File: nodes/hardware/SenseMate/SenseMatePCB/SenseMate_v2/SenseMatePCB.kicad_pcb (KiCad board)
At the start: 2 copper layers, 43.4 x 60 mm, 17 parts, among them J1 Conn_01x04, J2 Conn_02x06_Counter_Clockwise 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, J3 Conn_Coaxial, M1 Motor_DC, Q1 2SC1815, Q2 2SC1815, SW5 SW_DPDT_x2, U1 XIAO-nRF52840-Plus-SMD, U2 RFM95W-868S2

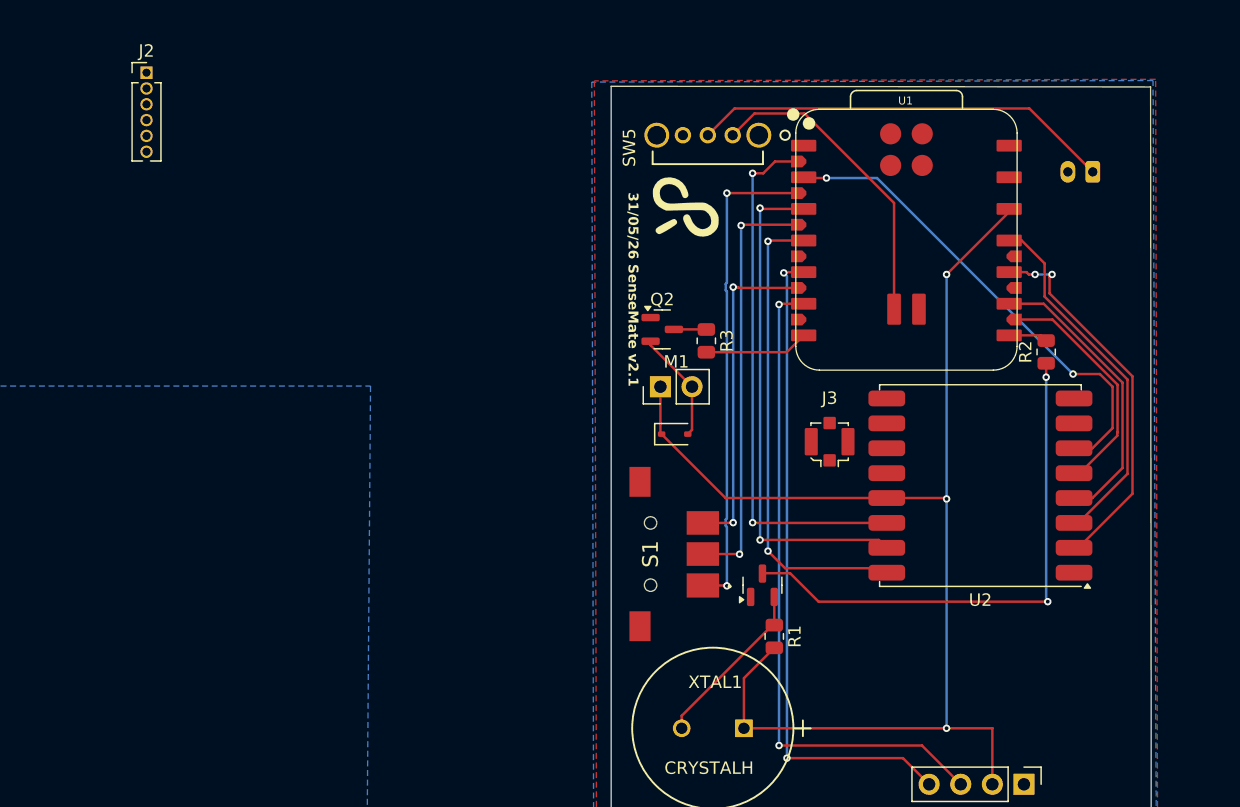
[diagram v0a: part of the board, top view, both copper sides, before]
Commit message: sensemate pcb v2.2: optimized routing further
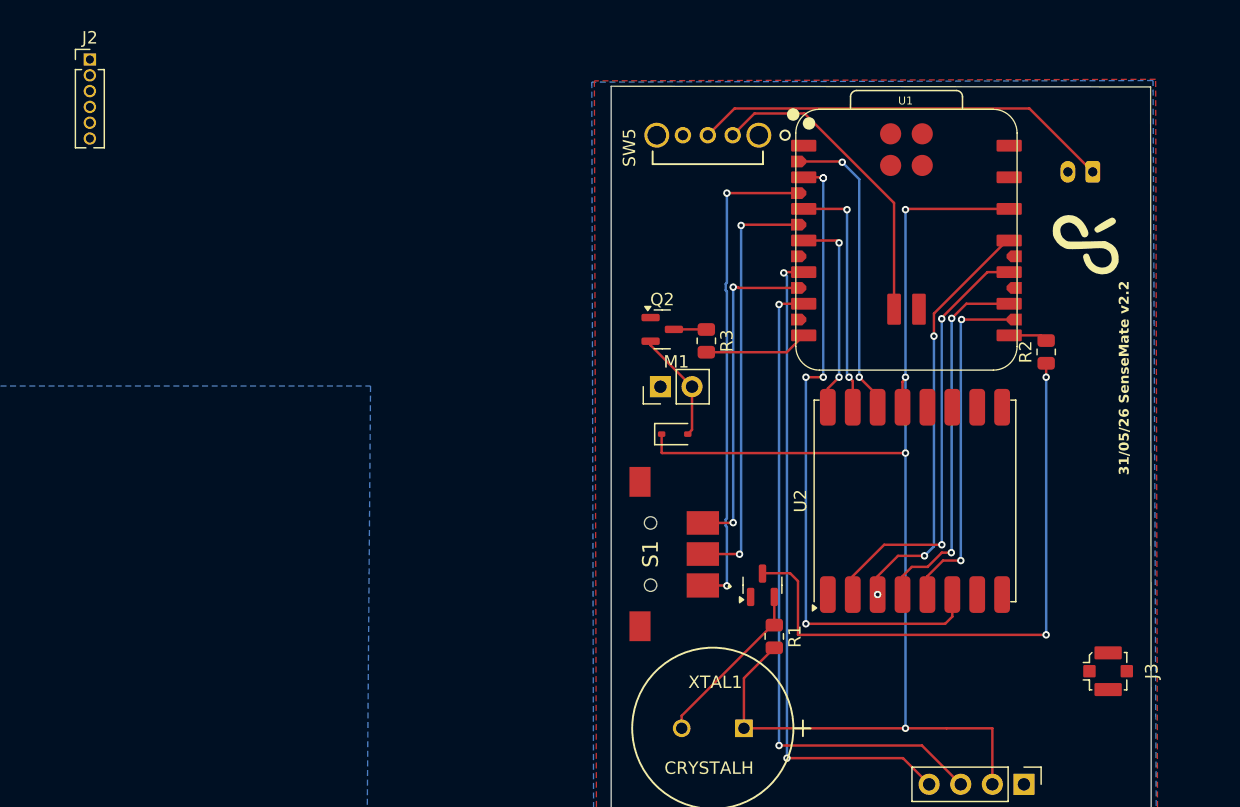
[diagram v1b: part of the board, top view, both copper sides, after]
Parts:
- moved G*** 32.2 mm to (116.5, 37.1), turned to 90 degrees
- moved J3 29.0 mm to (118.3, 73.9), turned to 90 degrees
- moved U2 5.40 mm to (102.7, 60.2), turned to 90 degrees
- moved J2 4.67 mm to (36.4, 24.8)
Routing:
- net LoRa_DIO2: track 38.1 -> 16.5 mm
- net LoRa_DIO1: track 40.6 -> 19.8 mm
- net LoRa_DIO0: track 43.0 -> 24.4 mm
- net LoRa_RST: track 38.9 -> 52.6 mm, vias 2 -> 5
- net LoRa_NSS: track 19.3 -> 28.4 mm, vias 0 -> 2
- net LoRa_SCK: track 23.5 -> 30.1 mm, vias 0 -> 2
- net Net-(Q1-B): track 43.0 -> 49.2 mm
- net LoRa_MOSI: track 29.2 -> 34.2 mm, vias 0 -> 3
- net LoRa_MISO: track 30.5 -> 34.9 mm
- net +3V3: track 104.7 -> 105.6 mm, vias 3 -> 4
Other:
- board text added: "31/05/26 SenseMate v2.2"
- board text removed: "31/05/26 SenseMate v2.1"

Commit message: Update SenseMatePCB.kicad_pcb
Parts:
- moved J3 20.7 mm to (116.2, 53.3)
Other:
- board text added: "01/06/26 SenseMate v2.2"
- board text removed: "31/05/26 SenseMate v2.2"
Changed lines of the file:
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@@
 	(footprint "Connector_Coaxial:U.FL_Molex_MCRF_73412-0110_Vertical"
 		(layer "F.Cu")
-		(at 118.261 73.914 90)
+		(at 116.181 53.34 90)
 		(descr "Molex Microcoaxial RF Connectors (MCRF), mates Hirose U.FL, (http://www.molex.com/pdm_docs/sd/734120110_sd.pdf)")
 		(tags "mcrf hirose ufl u.fl microcoaxial")
@@
 		(layer "Edge.Cuts")
 	)
-	(gr_text "31/05/26 SenseMate v2.2"
+	(gr_text "01/06/26 SenseMate v2.2"
 		(at 120.015 58.166 90)
 		(layer "F.SilkS")

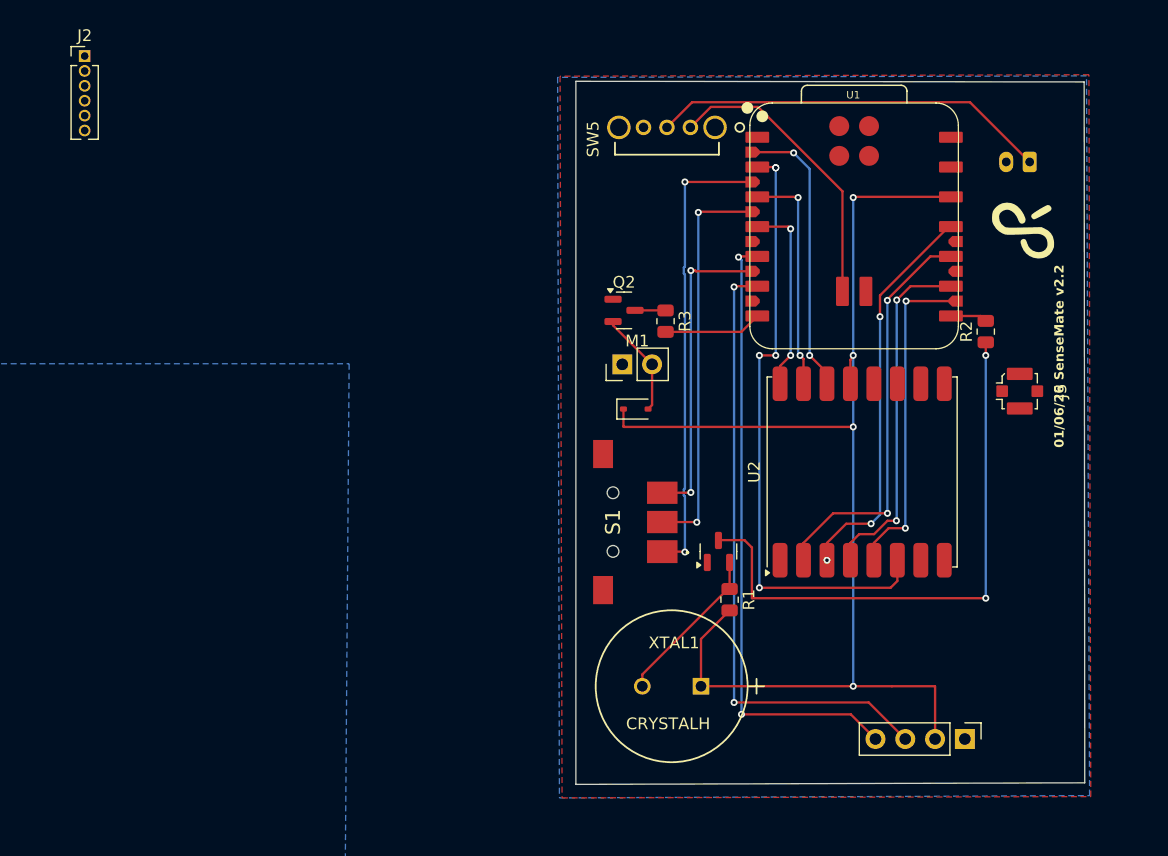
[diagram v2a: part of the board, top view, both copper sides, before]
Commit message: nodes/hardware/PCB: save some space with different arrangement
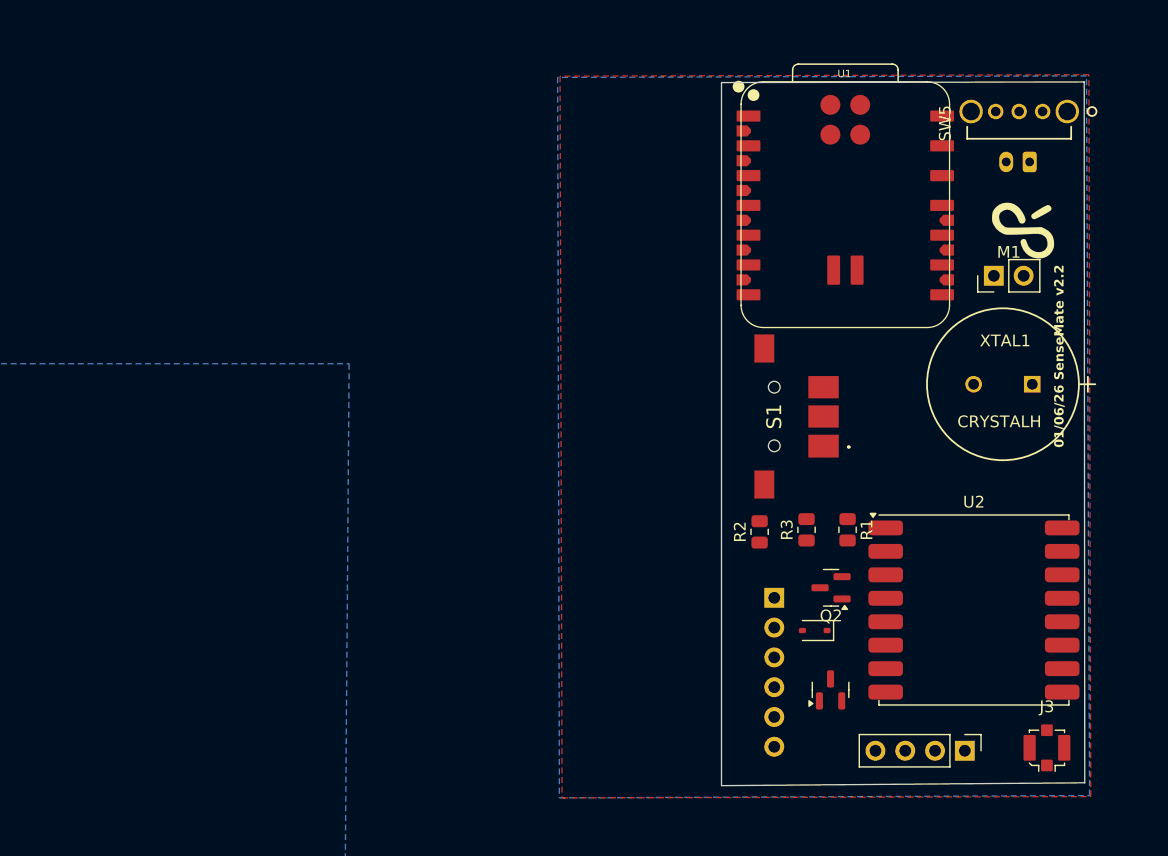
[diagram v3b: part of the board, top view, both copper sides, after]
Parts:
- J2: footprint Connector_PinHeader_1.27mm:PinHeader_1x06_P1.27mm_Vertical -> Connector_PinSocket_2.54mm:PinSocket_1x06_P2.54mm_Vertical; moved to B.Cu
- moved J2 74.8 mm to (95.2, 71.0), turned to 180 degrees
- moved XTAL1 38.2 mm to (117.2, 52.8)
- moved M1 32.6 mm to (114.0, 43.5)
- moved J3 30.5 mm to (118.5, 83.8), turned to 180 degrees
- moved SW5 30.1 mm to (118.1, 29.5)
- moved Q2 29.5 mm to (100.1, 70.1), turned to 180 degrees
- moved R2 25.8 mm to (94.0, 65.3)
- moved D1 24.3 mm to (98.7, 73.8), turned to 180 degrees
- moved R3 21.5 mm to (98.0, 65.2), turned to 90 degrees
- moved S1 16.4 mm to (95.2, 55.5)
- moved Q1 15.2 mm to (100.0, 78.8)
- moved U2 15.1 mm to (112.3, 72.0), turned to 0 degrees
- moved R1 11.7 mm to (101.5, 65.2)
- moved U1 1.96 mm to (101.3, 37.5)
- moved J1 1.00 mm to (111.5, 84.0)
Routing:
- net +3V3: track 105.6 -> 0.00 mm, vias 4 -> 0
- net SCL: track 53.3 -> 0.00 mm, vias 2 -> 0
- net SDA: track 53.0 -> 0.00 mm, vias 2 -> 0
- net LoRa_RST: track 52.6 -> 0.00 mm, vias 5 -> 0
- net Net-(Q1-B): track 49.2 -> 0.00 mm, vias 2 -> 0
- net TMB1: track 39.6 -> 0.00 mm, vias 2 -> 0
- net LoRa_MISO: track 34.9 -> 0.00 mm, vias 2 -> 0
- net LoRa_MOSI: track 34.2 -> 0.00 mm, vias 3 -> 0
- net TMBT1: track 34.1 -> 0.00 mm, vias 2 -> 0
- net Net-(BT1-+): track 33.9 -> 0.00 mm
- net LoRa_SCK: track 30.1 -> 0.00 mm, vias 2 -> 0
- net LoRa_NSS: track 28.4 -> 0.00 mm, vias 2 -> 0
- net TMB2: track 26.7 -> 0.00 mm, vias 2 -> 0
- net VBAT: track 25.2 -> 0.00 mm
- net LoRa_DIO0: track 24.4 -> 0.00 mm, vias 2 -> 0
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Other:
- board size 43.4 x 60 mm -> 31 x 60 mm

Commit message: finished tracing
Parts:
- removed J2: Conn_02x06_Counter_Clockwise (PogoPin), Connector_PinSocket_2.54mm:PinSocket_1x06_P2.54mm_Vertical
- added J5: Conn_01x06_Pin, Connector_PinHeader_2.54mm:PinHeader_1x06_P2.54mm_Vertical, F.Cu at (94.0, 50.8)
- moved D1 23.6 mm to (104.1, 50.8)
- moved Q1 20.8 mm to (104.7, 58.5)
- moved S1 18.2 mm to (94.0, 73.7)
- moved Q2 15.6 mm to (101.6, 54.6)
- moved R3 15.5 mm to (101.2, 50.0)
- moved R2 15.2 mm to (104.8, 54.6)
- moved R1 11.9 mm to (107.0, 54.6), turned to 90 degrees
- moved G*** 9.62 mm to (125.7, 34.5)
- moved M1 4.67 mm to (118.6, 44.1), turned to 180 degrees
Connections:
- J3 pad 1: unconnected-(J3-In-Pad1) -> ANT
- J3 pad 2: Net-(J3-Ext) -> GND
- U1 pad 1: unconnected-(U1-P0.02_A0_D0-Pad1) -> BUZ_EN
- U1 pad 14: unconnected-(U1-VBUS-Pad14) -> Pogo VBUS
- U1 pad 18: Pogo Pins -> TMB2
- U1 pad 19: TMB2 -> VIB_EN
- U1 pad 24: unconnected-(U1-SWDIO-Pad24) -> Pogo SWDIO
- U1 pad 25: unconnected-(U1-SWDCLK-Pad25) -> Pogo SWDCLK
- U1 pad 7: VIB_EN -> Pogo TX
- U1 pad 8: BUZ_EN -> Pogo RX
- U2 pad 9: Net-(J3-Ext) -> ANT
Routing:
- net +3V3: track 0.00 -> 84.0 mm, vias 0 -> 3
- net LoRa_RST: track 0.00 -> 68.9 mm, vias 0 -> 4
- net LoRa_DIO0: track 0.00 -> 64.7 mm, vias 0 -> 8
- net LoRa_DIO1: track 0.00 -> 58.6 mm, vias 0 -> 6
- net LoRa_DIO2: track 0.00 -> 54.6 mm, vias 0 -> 6
- net SDA: track 0.00 -> 51.1 mm, vias 0 -> 2
- net SCL: track 0.00 -> 50.1 mm, vias 0 -> 2
- net Pogo SWDIO: track 0.00 -> 48.9 mm, vias 0 -> 3
- net TMB1: track 0.00 -> 46.7 mm, vias 0 -> 2
- net Pogo SWDCLK: track 0.00 -> 46.4 mm, vias 0 -> 3
- net TMBT1: track 0.00 -> 42.7 mm, vias 0 -> 2
- net LoRa_MOSI: track 0.00 -> 42.6 mm, vias 0 -> 2
- net LoRa_SCK: track 0.00 -> 39.2 mm, vias 0 -> 2
- net LoRa_MISO: track 0.00 -> 37.8 mm, vias 0 -> 2
- net TMB2: track 0.00 -> 37.2 mm, vias 0 -> 2
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
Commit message: castellations almost done
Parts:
- added J2: Conn_01x12_Pin, SenseMateLibrary:Castellated_1x12_2.00mm, F.Cu at (92.0, 42.2)
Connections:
- U1 pad 20: unconnected-(U1-P0.31_D16_BAT-Pad20) -> P0.31
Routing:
- net P0.31: track 0.00 -> 8.91 mm
- net SCL: track 50.1 -> 58.9 mm
- net VIB_EN: track 16.5 -> 23.9 mm
- net SDA: track 51.1 -> 58.5 mm
- net TMB2: track 37.2 -> 43.2 mm
- net LoRa_DIO2: track 54.6 -> 60.5 mm
- net LoRa_DIO1: track 58.6 -> 63.5 mm
- net TMBT1: track 42.7 -> 47.5 mm
- net LoRa_RST: track 68.9 -> 73.2 mm
- net BUZ_EN: track 35.3 -> 39.5 mm
- net TMB1: track 46.7 -> 50.9 mm
- net LoRa_DIO0: track 64.7 -> 68.3 mm
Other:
- board size 31 x 60 mm -> 32.8 x 59.8 mm

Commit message: SENSEMATE V3 DONE
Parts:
- added J4: Conn_01x06_Pin, SenseMateLibrary:Castellated_1x6_2.00mm, F.Cu at (92.0, 67.2)
- added J6: Conn_01x02_Pin, SenseMateLibrary:Castellated_1x2_2.00mm, F.Cu at (124.7, 70.3)
- moved G*** 10.5 mm to (115.3, 35.0)
- moved S1 3.02 mm to (92.2, 76.1)
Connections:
- U1 pad 22: unconnected-(U1-P1.05_D18_MISO1-Pad22) -> SPI_MISO1
- U1 pad 23: unconnected-(U1-P1.07_D19_MOSI1-Pad23) -> SPI_MOSI1
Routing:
- net SPI_MOSI1: track 0.00 -> 26.5 mm, vias 0 -> 4
- net SPI_MISO1: track 0.00 -> 25.4 mm, vias 0 -> 5
- net Pogo TX: track 11.6 -> 21.8 mm, vias 0 -> 2
- net Pogo VBUS: track 35.0 -> 41.5 mm
- net Pogo RX: track 22.8 -> 28.9 mm
- net GND: track 0.00 -> 5.71 mm
- net Pogo SWDIO: track 48.9 -> 54.4 mm
- net Pogo SWDCLK: track 46.4 -> 51.7 mm
- net TMB1: track 50.9 -> 53.7 mm
- net TMBT1: track 47.5 -> 50.1 mm
- net TMB2: track 43.2 -> 45.4 mm
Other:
- board text added: "11/06/26 SenseMate v3"
- board text removed: "01/06/26 SenseMate v2.2"

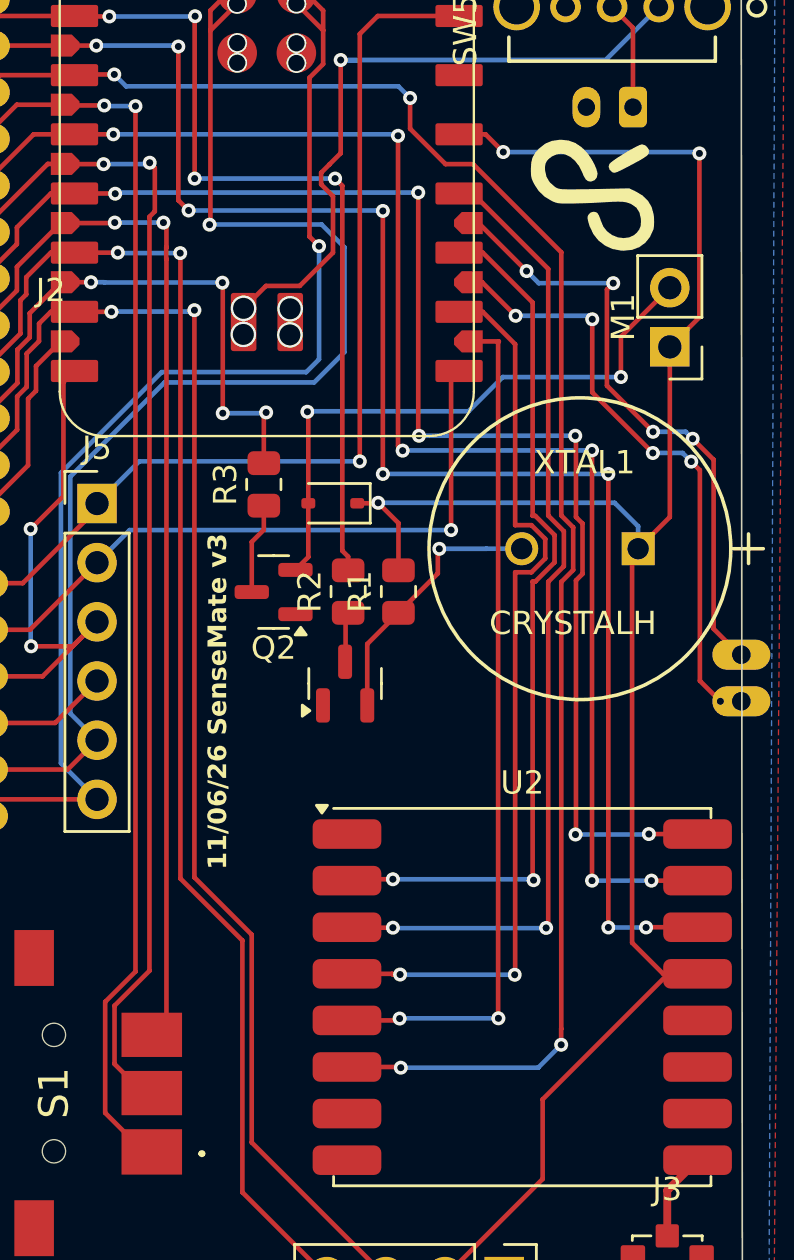
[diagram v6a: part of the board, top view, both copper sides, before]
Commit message: Changed SMD Transistor to SS8050 to fix Problem with wrong fields
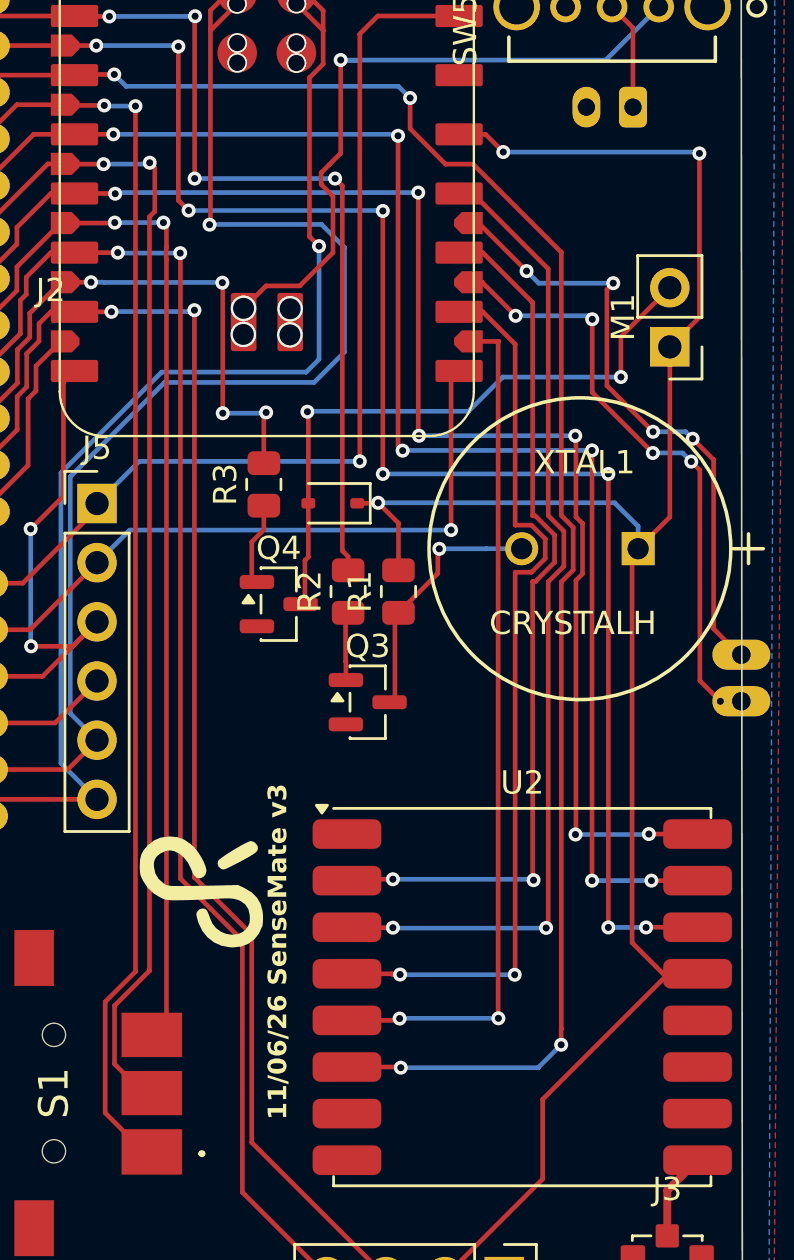
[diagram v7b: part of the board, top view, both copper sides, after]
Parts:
- removed Q1, Q2: 2SC1815, Package_TO_SOT_SMD:SOT-23
- added Q3: SS8050, Package_TO_SOT_SMD:SOT-23, F.Cu at (105.6, 59.3)
- added Q4: SS8050, Package_TO_SOT_SMD:SOT-23, F.Cu at (101.8, 55.1)
- moved G*** 34.3 mm to (98.5, 64.9)
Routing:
- net Net-(D1-A): track 25.8 -> 27.2 mm
- net Net-(Q3-B): track 2.15 -> 2.94 mm
- net Net-(Q3-C): track 11.5 -> 11.0 mm
